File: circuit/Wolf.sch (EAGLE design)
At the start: 14 parts, among them IC1 74LS595N, K1 SNES, M1 ARDUINO-NANO-3.0

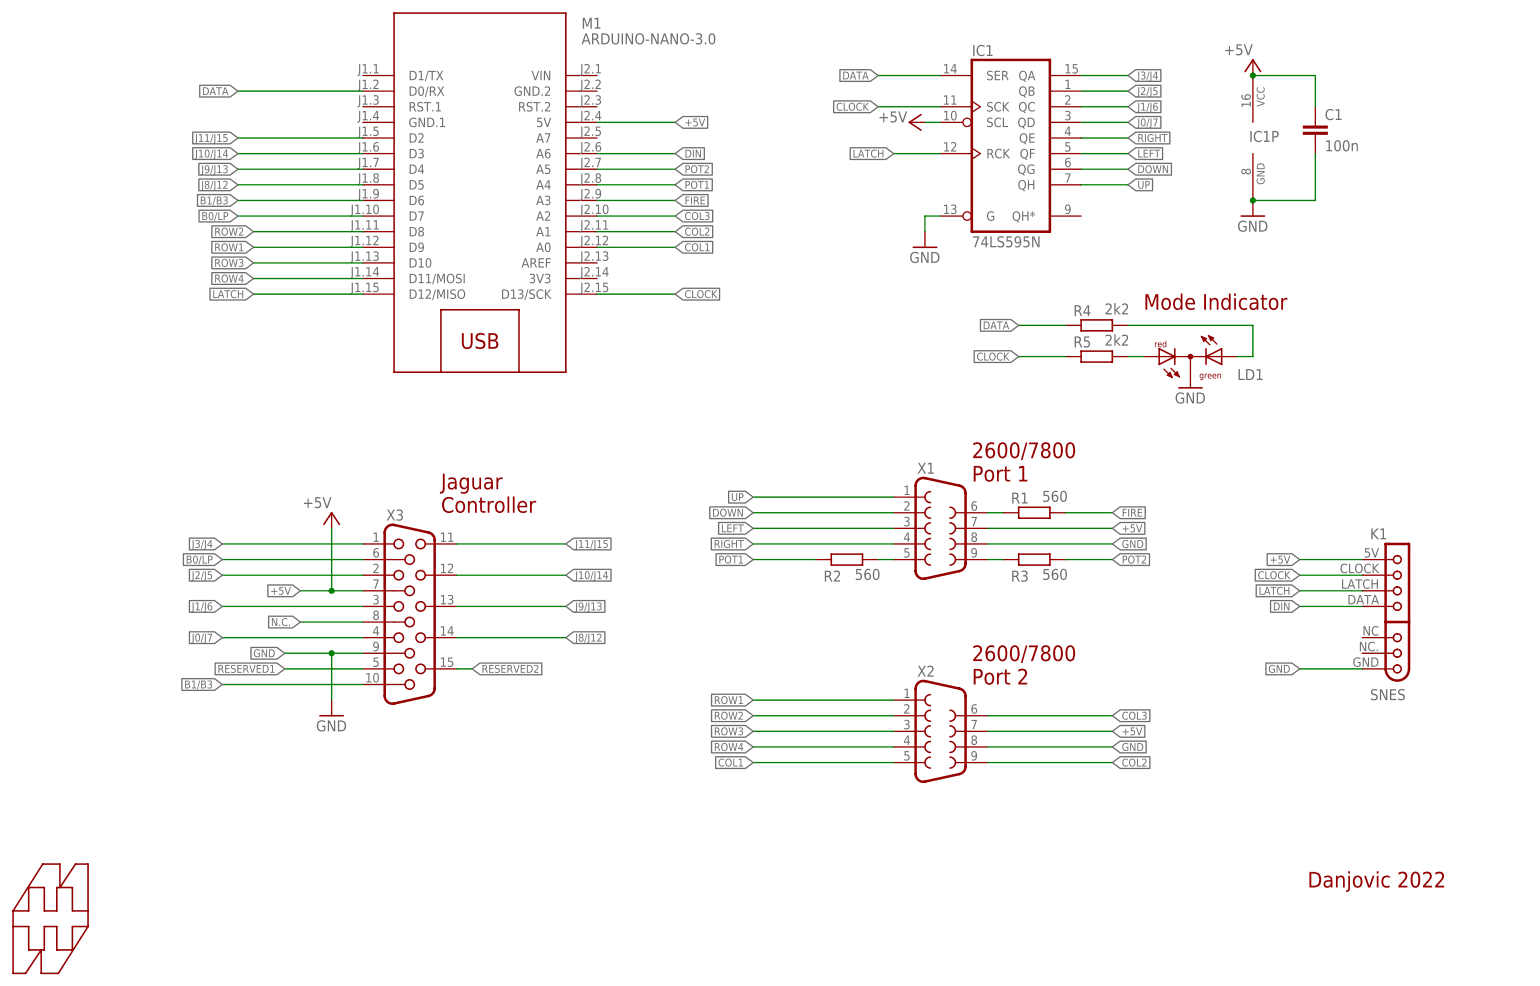
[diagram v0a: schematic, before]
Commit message: added contention protect resistors
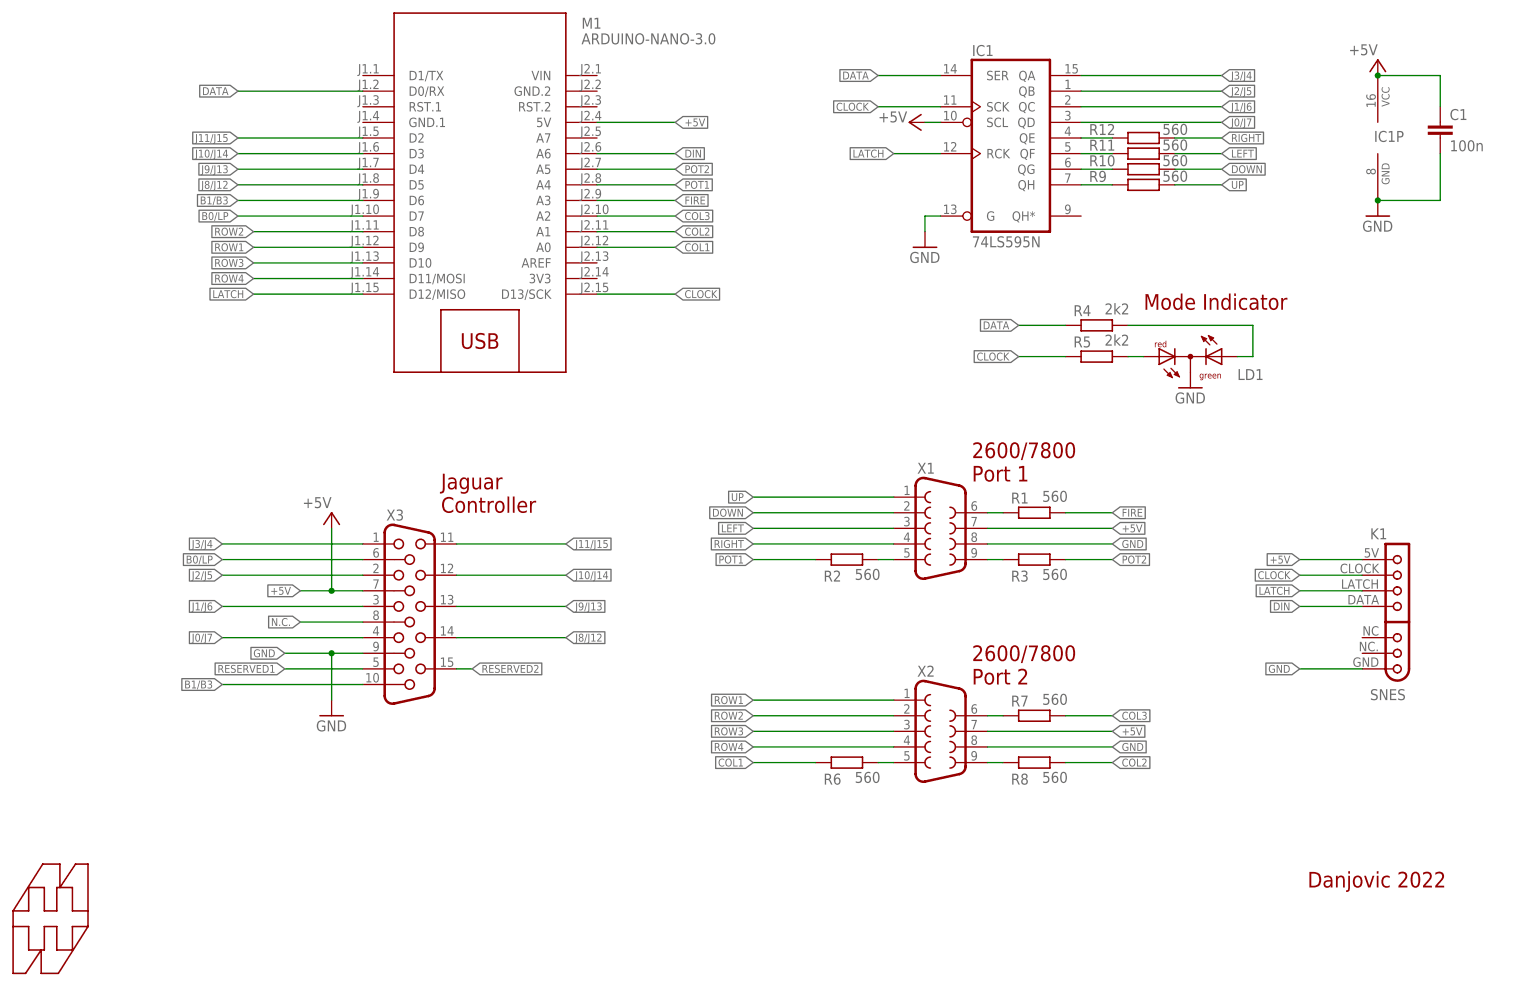
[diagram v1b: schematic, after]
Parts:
- added R10, R11, R12, R6, R7, R8, R9: 560, rcl:R-EU_0204/7
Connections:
- new net R_COL1: R6.2, X2.5
- new net R_COL2: R8.1, X2.9
- new net R_COL3: R7.1, X2.6
- new net R_DOWN: IC1A.QG, R10.1
- new net R_LEFT: IC1A.QF, R11.1
- new net R_RIGHT: IC1A.QE, R12.1
- new net R_UP: IC1A.QH, R9.1
- net COL1: now also R6.1; no longer X2.5
- net COL2: now also R8.2; no longer X2.9
- net COL3: now also R7.2; no longer X2.6
- net DOWN: now also R10.2; no longer IC1A.QG
- net LEFT: now also R11.2; no longer IC1A.QF
- net RIGHT: now also R12.2; no longer IC1A.QE
- net UP: now also R9.2; no longer IC1A.QH
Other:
- moved on the sheet: C1, IC1P

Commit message: updated pcb
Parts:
- K1: device snes_breakout:SNESG -> snes_breakout:SNES-R
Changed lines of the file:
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@@
 <grid distance="0.1" unitdist="inch" unit="inch" style="lines" multiple="1" display="no" altdistance="0.01" altunitdist="inch" altunit="inch"/>
 <layers>
-<layer number="1" name="Top" color="4" fill="1" visible="no" active="no"/>
-<layer number="16" name="Bottom" color="1" fill="1" visible="no" active="no"/>
-<layer number="17" name="Pads" color="2" fill="1" visible="no" active="no"/>
-<layer number="18" name="Vias" color="2" fill="1" visible="no" active="no"/>
-<layer number="19" name="Unrouted" color="6" fill="1" visible="no" active="no"/>
-<layer number="20" name="Dimension" color="15" fill="1" visible="no" active="no"/>
-<layer number="21" name="tPlace" color="7" fill="1" visible="no" active="no"/>
-<layer number="22" name="bPlace" color="7" fill="1" visible="no" active="no"/>
-<layer number="23" name="tOrigins" color="15" fill="1" visible="no" active="no"/>
-<layer number="24" name="bOrigins" color="15" fill="1" visible="no" active="no"/>
-<layer number="25" name="tNames" color="7" fill="1" visible="no" active="no"/>
-<layer number="26" name="bNames" color="7" fill="1" visible="no" active="no"/>
-<layer number="27" name="tValues" color="7" fill="1" visible="no" active="no"/>
-<layer number="28" name="bValues" color="7" fill="1" visible="no" active="no"/>
+<layer number="1" name="Top" color="4" fill="1" visible="yes" active="no"/>
+<layer number="16" name="Bottom" color="1" fill="1" visible="yes" active="no"/>
+<layer number="17" name="Pads" color="2" fill="1" visible="yes" active="no"/>
+<layer number="18" name="Vias" color="2" fill="1" visible="yes" active="no"/>
+<layer number="19" name="Unrouted" color="6" fill="1" visible="yes" active="no"/>
+<layer number="20" name="Dimension" color="15" fill="1" visible="yes" active="no"/>
+<layer number="21" name="tPlace" color="7" fill="1" visible="yes" active="no"/>
+<layer number="22" name="bPlace" color="7" fill="1" visible="yes" active="no"/>
+<layer number="23" name="tOrigins" color="15" fill="1" visible="yes" active="no"/>
+<layer number="24" name="bOrigins" color="15" fill="1" visible="yes" active="no"/>
+<layer number="25" name="tNames" color="7" fill="1" visible="yes" active="no"/>
+<layer number="26" name="bNames" color="7" fill="1" visible="yes" active="no"/>
+<layer number="27" name="tValues" color="7" fill="1" visible="yes" active="no"/>
+<layer number="28" name="bValues" color="7" fill="1" visible="yes" active="no"/>
 <layer number="29" name="tStop" color="7" fill="3" visible="no" active="no"/>
 <layer number="30" name="bStop" color="7" fill="6" visible="no" active="no"/>
@@
 <layer number="35" name="tGlue" color="7" fill="4" visible="no" active="no"/>
 <layer number="36" name="bGlue" color="7" fill="5" visible="no" active="no"/>
-<layer number="37" name="tTest" color="7" fill="1" visible="no" active="no"/>
-<layer number="38" name="bTest" color="7" fill="1" visible="no" active="no"/>
+<layer number="37" name="tTest" color="7" fill="1" visible="yes" active="no"/>
+<layer number="38" name="bTest" color="7" fill="1" visible="yes" active="no"/>
 <layer number="39" name="tKeepout" color="4" fill="11" visible="no" active="no"/>
 <layer number="40" name="bKeepout" color="1" fill="11" visible="no" active="no"/>
@@
 <layer number="44" name="Drills" color="7" fill="1" visible="no" active="no"/>
 <layer number="45" name="Holes" color="7" fill="1" visible="no" active="no"/>
-<layer number="46" name="Milling" color="3" fill="1" visible="no" active="no"/>
-<layer number="47" name="Measures" color="7" fill="1" visible="no" active="no"/>
-<layer number="48" name="Document" color="7" fill="1" visible="no" active="no"/>
-<layer number="49" name="Reference" color="7" fill="1" visible="no" active="no"/>
-<layer number="51" name="tDocu" color="7" fill="1" visible="no" active="no"/>
-<layer number="52" name="bDocu" color="7" fill="1" visible="no" active="no"/>
+<layer number="46" name="Milling" color="3" fill="1" visible="yes" active="no"/>
+<layer number="47" name="Measures" color="7" fill="1" visible="yes" active="no"/>
+<layer number="48" name="Document" color="7" fill="1" visible="yes" active="no"/>
+<layer number="49" name="Reference" color="7" fill="1" visible="yes" active="no"/>
+<layer number="51" name="tDocu" color="7" fill="1" visible="yes" active="no"/>
+<layer number="52" name="bDocu" color="7" fill="1" visible="yes" active="no"/>
 <layer number="90" name="Modules" color="5" fill="1" visible="yes" active="yes"/>
 <layer number="91" name="Nets" color="2" fill="1" visible="yes" active="yes"/>
@@
 <part name="X2" library="con-subd" deviceset="F09" device="H"/>
 <part name="M1" library="diy-modules" deviceset="ARDUINO-NANO-3.0" device=""/>
-<part name="K1" library="snes_breakout" deviceset="SNES" device="G" value="SNES"/>
+<part name="K1" library="snes_breakout" deviceset="SNES" device="-R" value="SNES"/>
 <part name="FRAME1" library="frames" deviceset="A4L-LOC" device=""/>
 <part name="IC1" library="74xx-us" deviceset="74*595" device="N" technology="LS" value="74LS595N"/>

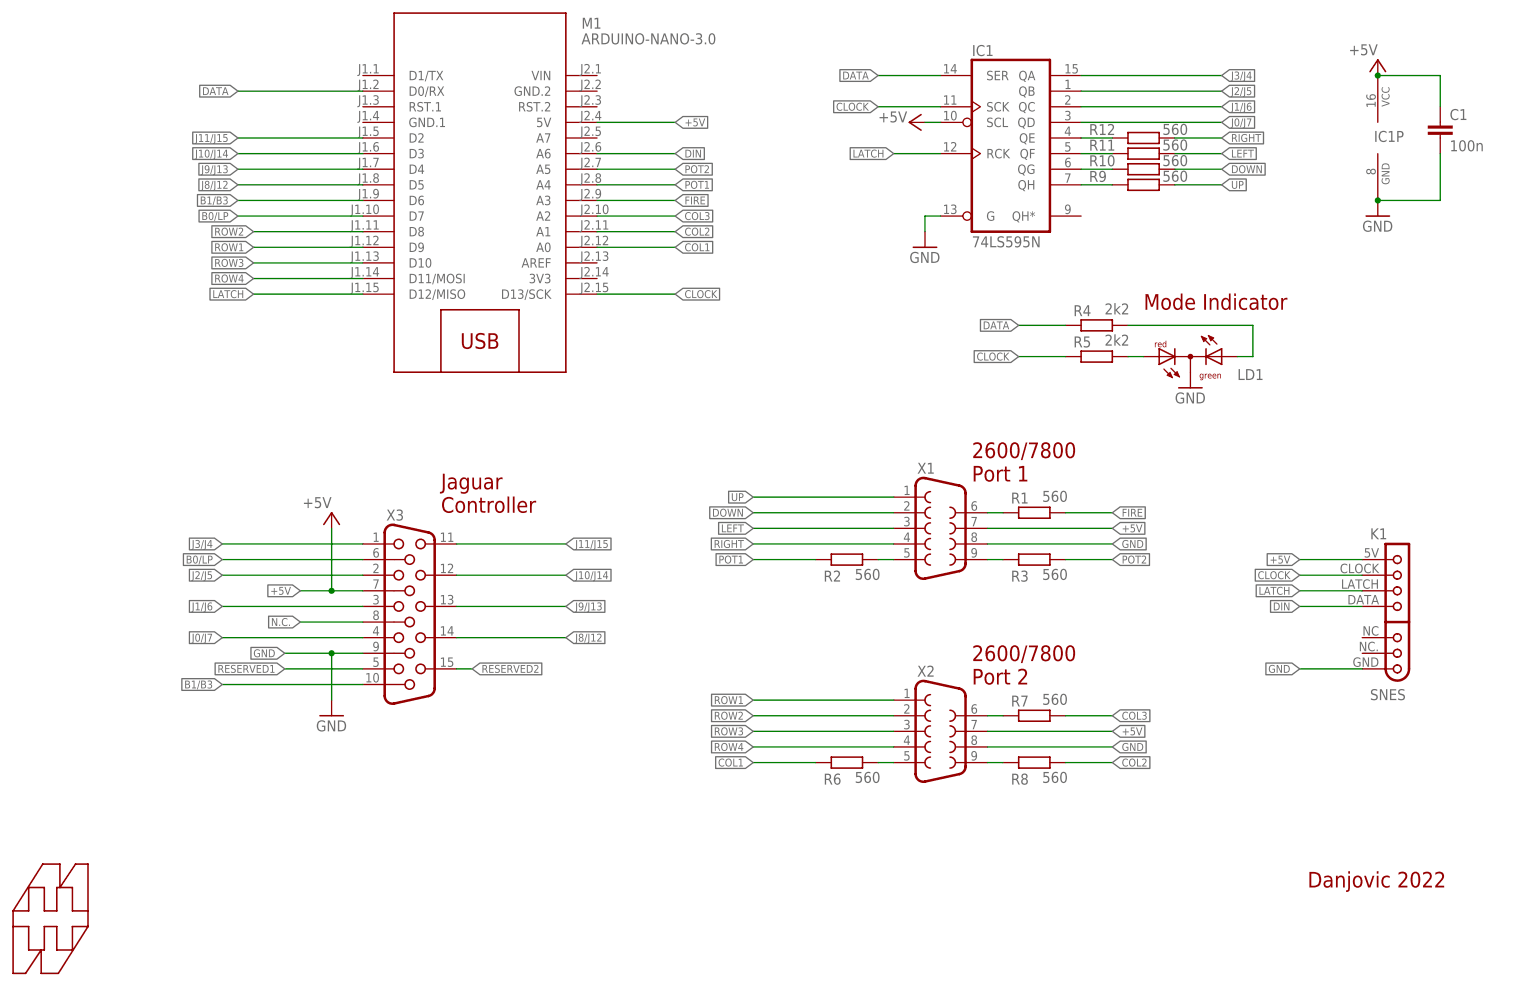
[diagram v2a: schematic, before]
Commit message: Added missing connection to GND
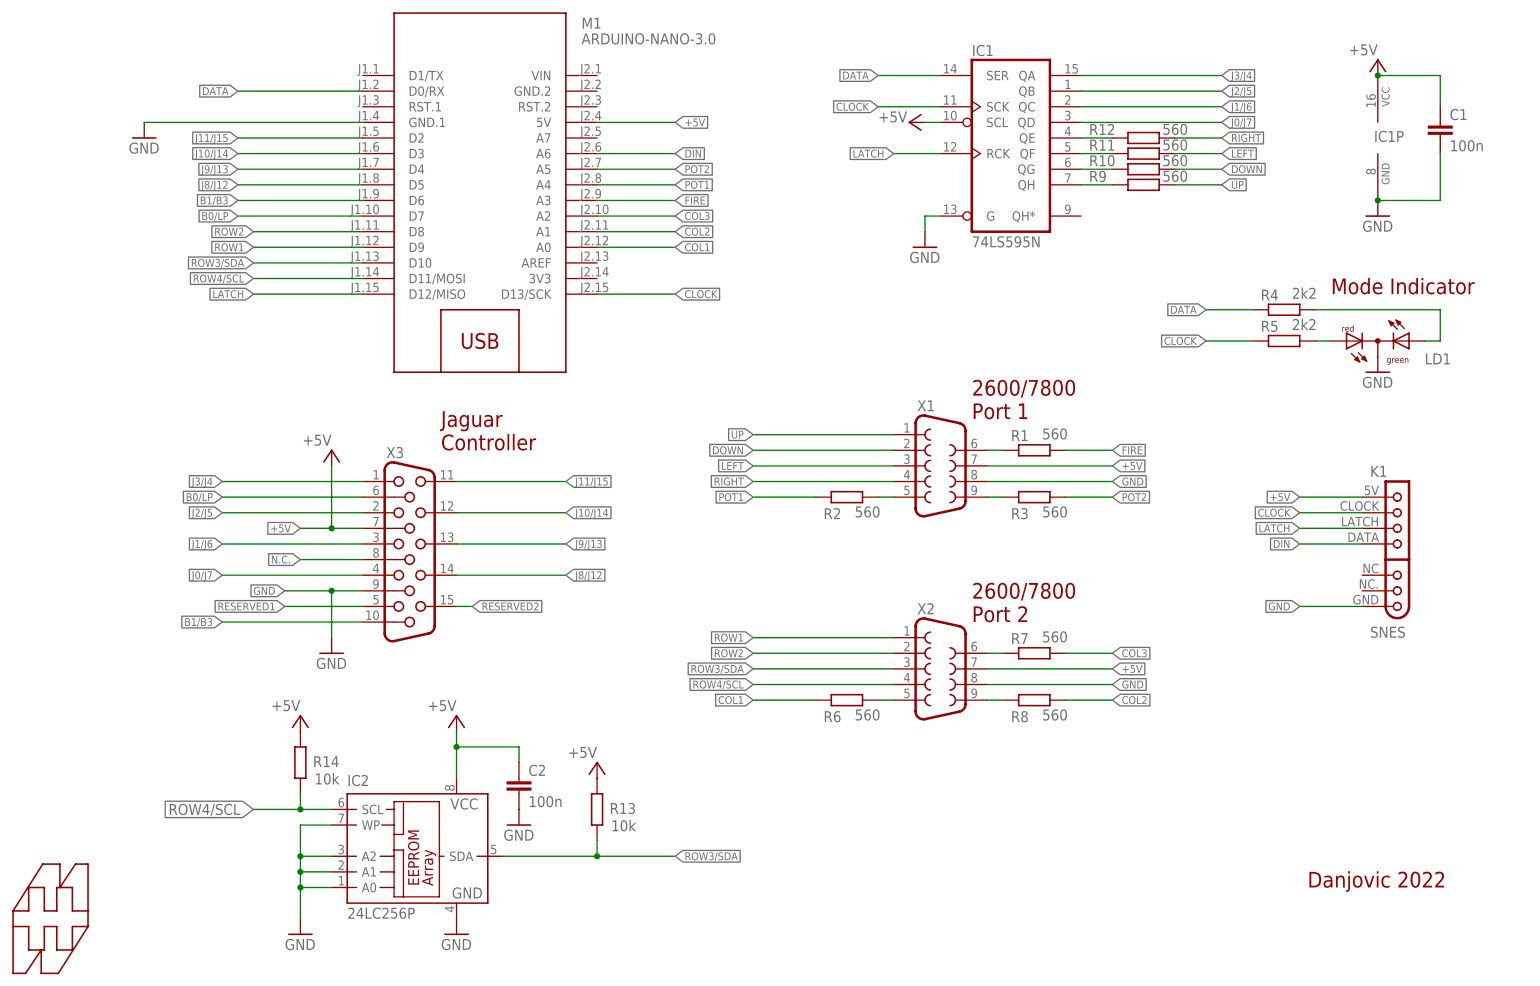
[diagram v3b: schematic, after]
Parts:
- added C2: 100n, rcl:C-EU050-024X044
- added IC2: 24LC256P, microchip:24LC256P
- added R13, R14: 10k, rcl:R-EU_0204/7
- X1, X2: device con-subd:F09H -> con-subd:F09HP
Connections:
- removed net ROW3: M1.D10, X2.3
- removed net ROW4: M1.D11/MOSI, X2.4
- new net ROW3/SDA: IC2.SDA, M1.D10, R13.1, X2.3
- new net ROW4/SCL: IC2.SCL, M1.D11/MOSI, R14.1, X2.4
- net +5V: now also C2.1, IC2.VCC, R13.2, R14.2
- net GND: now also C2.2, IC2.A0, IC2.A1, IC2.A2, IC2.GND, IC2.WP, M1.GND.1
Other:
- moved on the sheet: K1, LD1, R1, R2, R3, R4, R5, R6, R7, R8, X1, X2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

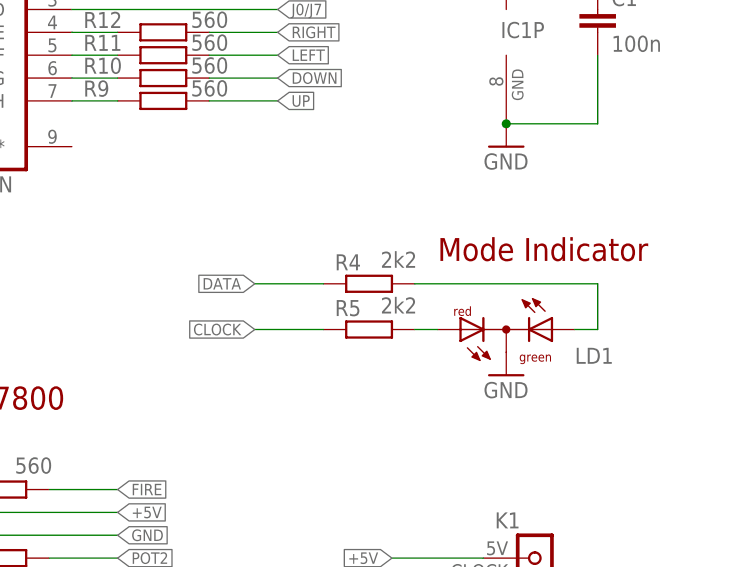
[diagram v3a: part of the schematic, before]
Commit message: Changed resistor for bicolor LED
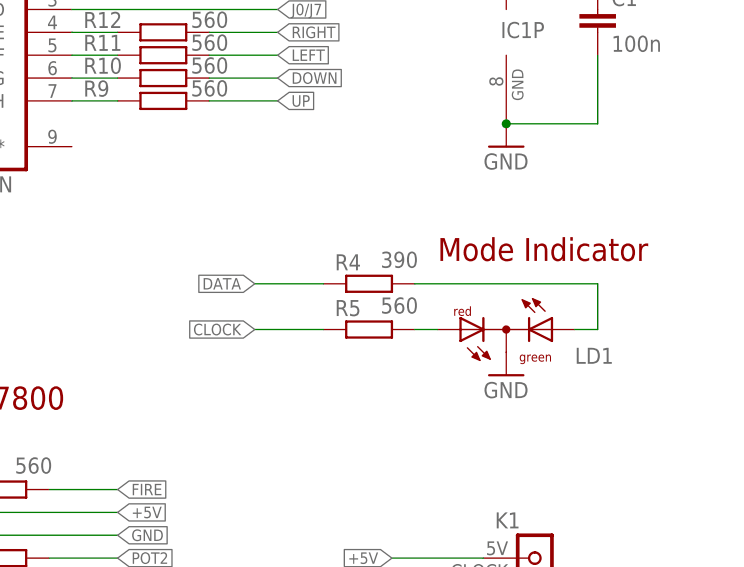
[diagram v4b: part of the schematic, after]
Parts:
- R4: value 2k2 -> 390
- R5: value 2k2 -> 560
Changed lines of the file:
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@@
 <part name="R2" library="rcl" deviceset="R-EU_" device="0204/7" value="560"/>
 <part name="R3" library="rcl" deviceset="R-EU_" device="0204/7" value="560"/>
-<part name="R4" library="rcl" deviceset="R-EU_" device="0204/7" value="2k2"/>
-<part name="R5" library="rcl" deviceset="R-EU_" device="0204/7" value="2k2"/>
+<part name="R4" library="rcl" deviceset="R-EU_" device="0204/7" value="390"/>
+<part name="R5" library="rcl" deviceset="R-EU_" device="0204/7" value="560"/>
 <part name="C1" library="rcl" deviceset="C-EU" device="050-024X044" value="100n"/>
 <part name="LD1" library="led" deviceset="DUOLED-RG-C" device=""/>
